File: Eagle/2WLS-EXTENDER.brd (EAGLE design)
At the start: 87 x 87 mm, 6 parts

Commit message: Add 2WLS EXTENDER and fix 2WLS PASSIVE solder mask
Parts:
- removed H10: MOUNT-PAD-ROUND3.3, holes:3,3-PAD
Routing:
- net 15V-: track 201.4 -> 236.4 mm
- net NGND: track 209.2 -> 192.3 mm
- net SDA: track 253.0 -> 237.5 mm
- net NC: track 199.8 -> 184.2 mm
- net 12V+: track 198.6 -> 183.0 mm
- net SCL: track 251.7 -> 236.1 mm
- net 5V+: track 198.6 -> 183.0 mm
- net 15V+: track 198.4 -> 183.0 mm
- net QGND: track 198.4 -> 183.0 mm
- net N$1: track 0.00 -> 7.62 mm
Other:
- board size 87 x 87 mm -> 87 x 79.1 mm
- board text added: "2WLS-EXTENDER R0 05/2025 DC"
- board text removed: "2WLS-PASSIVE R0 10/2023"

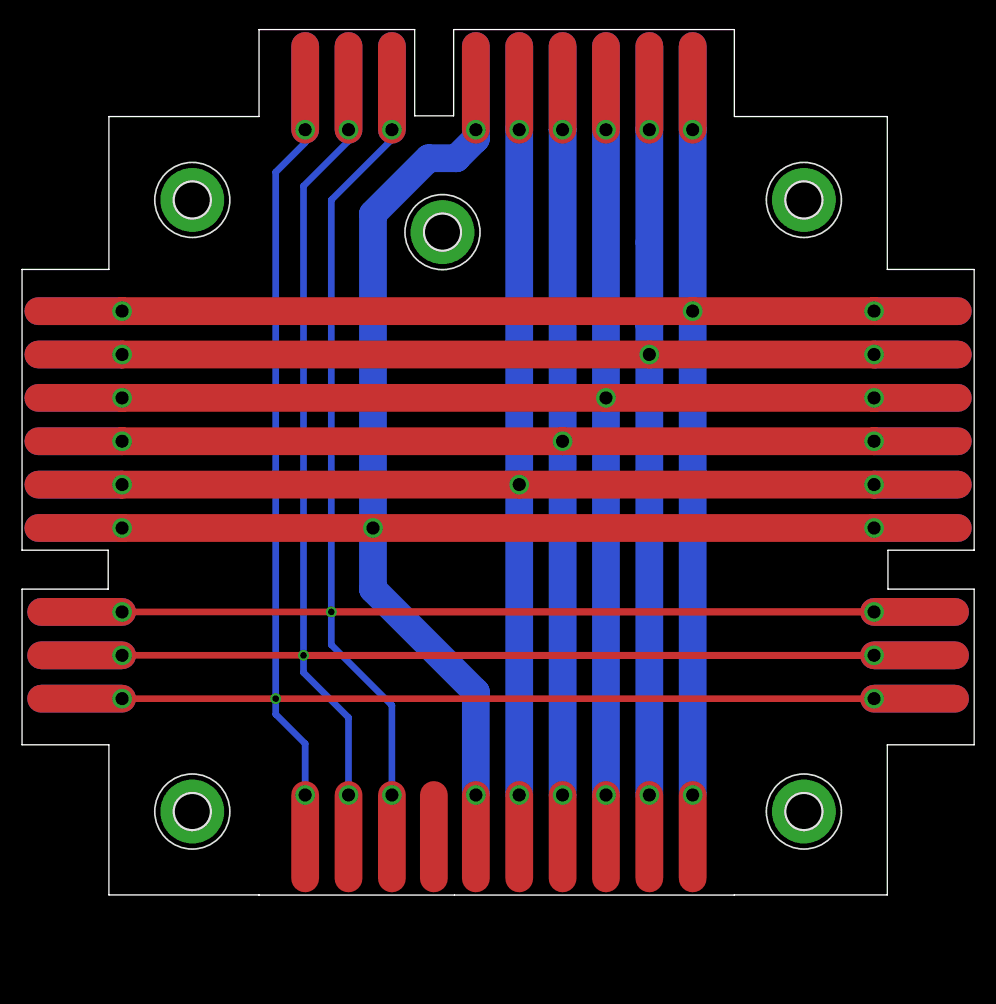
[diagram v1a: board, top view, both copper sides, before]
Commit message: Adjust dimensions to fit Keen case.
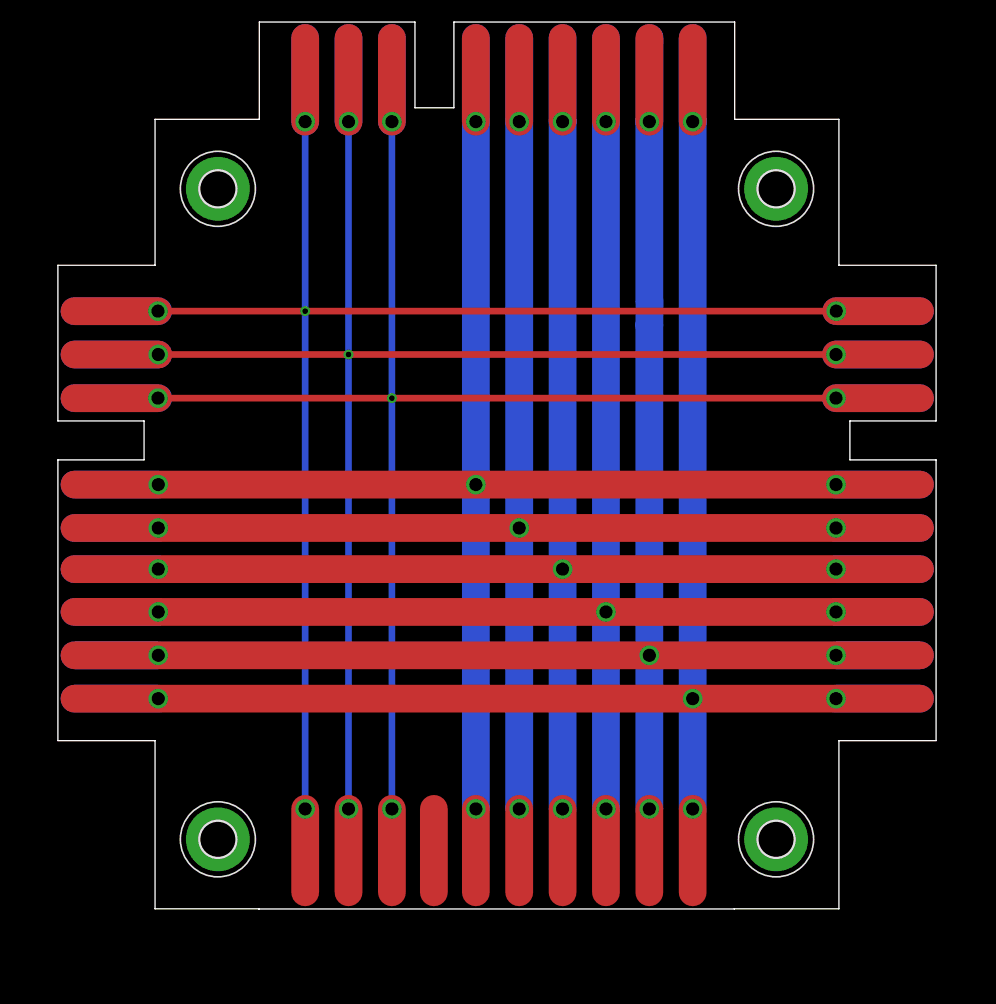
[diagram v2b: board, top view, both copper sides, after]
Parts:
- removed H15: MOUNT-PAD-ROUND3.3, holes:3,3-PAD
- moved H2 3.59 mm to (365.8, 5.08)
- moved H8 3.45 mm to (314.8, 5.08)
- moved H1 2.74 mm to (365.8, 64.5)
- moved H7 2.55 mm to (314.8, 64.5)
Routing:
- net SDA: track 237.5 -> 178.3 mm
- net SCL: track 236.1 -> 178.3 mm
- net NGND: track 192.3 -> 178.3 mm
- net 15V-: track 236.4 -> 227.6 mm
- net NC: track 184.2 -> 178.3 mm
- net QGND: track 183.0 -> 178.3 mm
- net 5V+: track 183.0 -> 178.3 mm
- net 15V+: track 183.0 -> 178.3 mm
- net 12V+: track 183.0 -> 178.3 mm
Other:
- board size 87 x 79.1 mm -> 80.2 x 81 mm
- board text added: "2WLS-EXTENDER R1 06/2025 DC"
- board text removed: "2WLS-EXTENDER R0 05/2025 DC"
